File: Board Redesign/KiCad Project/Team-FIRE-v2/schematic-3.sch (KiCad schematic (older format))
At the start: 27 parts, among them IC2 BTS500601TEAAUMA2, U8 TPS82140SILR

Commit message: Starting complete BOM generation
- Finished schematic(s)
- Started BOM information assignment for final BOM sent to NASA
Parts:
- gave numbers to parts that had none: 24

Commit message: Fixed libraries, added BOM info to most components
- Fixed MCP1826T library to be a part of Team-Fire library (not separate)
- Deleted useless library files for various pieces (such as ImportGuides, etc.)
- Fixed inductor value specification for boost converter
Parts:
- removed U8: TPS82140SILR, SIL0008D_SMD, symbol sw_reg:TPS82140SILR
- removed U9: MCP1826T-3302E_DC, Package_TO_SOT_SMD:SOT-223-5, symbol Team-FIRE:MCP1826T-3302E_DC
- added IC?: MCP1826T-3302E_DC, Team-FIRE:SOT127P706X180-6N, symbol Team-FIRE:MCP1826T-3302E_DC
- added U?: TPS82140, Package_LGA:Texas_MicroSiP-8-1EP_2.8x3.0mm_P0.65mm_EP1.1x1.9mm_SMD_ThermalVias, symbol Regulator_Switching:TPS82140
- J10: Height 4.34 -> (none); Manufacturer (none) -> Taoglas; Manufacturer_Name Taoglas -> (none); Mouser Part Number 960-PCBMMCXFSTJACKHT -> (none); Mouser Price/Stock https://www.mouser.com/Search/Refine.aspx?Keyword=960-PCBMM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 -> (none); Supplier PN (none) -> 960-PCBMMCXFSTJACKHT
- J9: Height 1.25 -> (none); Manufacturer (none) -> Hirose; Manufacturer PN (none) -> U.FL-R-SMT(10); Manufacturer_Name Hirose -> (none); Manufacturer_Part_Number U.FL-R-SMT(10) -> (none); Mouser Price/Stock https://www.mouser.com/Search/Refine.aspx?Keyword=798-U.FL-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 -> (none)
- TP1, TP2, TP3, TP4, TP5, TP6, TP7, TP8: footprint (none) -> TestPoint:TestPoint_Pad_D1.5mm
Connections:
- wire segments 78 -> 73
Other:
- moved on the sheet: C32, C33, C34, C35, R21, R22, R24, R25, TP1, TP2, TP3, TP4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

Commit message: Made a lot of changes...
- Added symbol, footprint for Micro USB B connector
- Fixed Flash Memory schematic
- Added details for many components
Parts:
- gave numbers to parts that had none: 2
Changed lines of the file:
@@
 PWR_EN
 $Comp
-L Regulator_Switching:TPS82140 U?
+L Regulator_Switching:TPS82140 U8
 U 1 1 5EB31C18
 P 7100 1650
-F 0 "U?" H 7100 2117 50  0000 C CNN
+F 0 "U8" H 7100 2117 50  0000 C CNN
 F 1 "TPS82140" H 7100 2026 50  0000 C CNN
 F 2 "Package_LGA:Texas_MicroSiP-8-1EP_2.8x3.0mm_P0.65mm_EP1.1x1.9mm_SMD_ThermalVias" H 7100 1000 50  0001 C CNN
@@
 $EndComp
 $Comp
-L power:GND #PWR?
+L power:GND #PWR04
 U 1 1 5EB3DB22
 P 7100 2050
-F 0 "#PWR?" H 7100 1800 50  0001 C CNN
+F 0 "#PWR04" H 7100 1800 50  0001 C CNN
 F 1 "GND" H 7105 1877 50  0000 C CNN
 F 2 "" H 7100 2050 50  0001 C CNN
@@
 	6600 1850 6600 1950
 $Comp
-L power:GND #PWR?
+L power:GND #PWR07
 U 1 1 5EB42A65
 P 6600 2250
-F 0 "#PWR?" H 6600 2000 50  0001 C CNN
+F 0 "#PWR07" H 6600 2000 50  0001 C CNN
 F 1 "GND" H 6605 2077 50  0000 C CNN
 F 2 "" H 6600 2250 50  0001 C CNN
@@
 Connection ~ 6500 1450
 $Comp
-L power:GND #PWR?
+L power:GND #PWR03
 U 1 1 5EB9233E
 P 6350 1850
-F 0 "#PWR?" H 6350 1600 50  0001 C CNN
+F 0 "#PWR03" H 6350 1600 50  0001 C CNN
 F 1 "GND" H 6355 1677 50  0000 C CNN
 F 2 "" H 6350 1850 50  0001 C CNN
@@
 Connection ~ 7800 1850
 $Comp
-L power:GND #PWR?
+L power:GND #PWR05
 U 1 1 5EBE5BFA
 P 7800 2200
-F 0 "#PWR?" H 7800 1950 50  0001 C CNN
+F 0 "#PWR05" H 7800 1950 50  0001 C CNN
 F 1 "GND" H 7805 2027 50  0000 C CNN
 F 2 "" H 7800 2200 50  0001 C CNN
@@
 	8100 2000 8100 2200
 $Comp
-L power:GND #PWR?
+L power:GND #PWR06
 U 1 1 5EBED12A
 P 8100 2200
-F 0 "#PWR?" H 8100 1950 50  0001 C CNN
+F 0 "#PWR06" H 8100 1950 50  0001 C CNN
 F 1 "GND" H 8105 2027 50  0000 C CNN
 F 2 "" H 8100 2200 50  0001 C CNN
@@
 	5950 2650 5950 950
 $Comp
-L Team-FIRE:MCP1826T-3302E_DC IC?
+L Team-FIRE:MCP1826T-3302E_DC IC1
 U 1 1 5EC035E3
 P 1650 3450
-F 0 "IC?" H 2350 3765 50  0000 C CNN
+F 0 "IC1" H 2350 3765 50  0000 C CNN
 F 1 "MCP1826T-3302E_DC" H 2350 3674 50  0000 C CNN
 F 2 "Team-FIRE:SOT127P706X180-6N" H 2900 3550 50  0001 L CNN
@@
 	3150 3650 3150 3750
 $Comp
-L power:GND #PWR?
+L power:GND #PWR08
 U 1 1 5EC0985C
 P 3150 3900
-F 0 "#PWR?" H 3150 3650 50  0001 C CNN
+F 0 "#PWR08" H 3150 3650 50  0001 C CNN
 F 1 "GND" H 3155 3727 50  0000 C CNN
 F 2 "" H 3150 3900 50  0001 C CNN

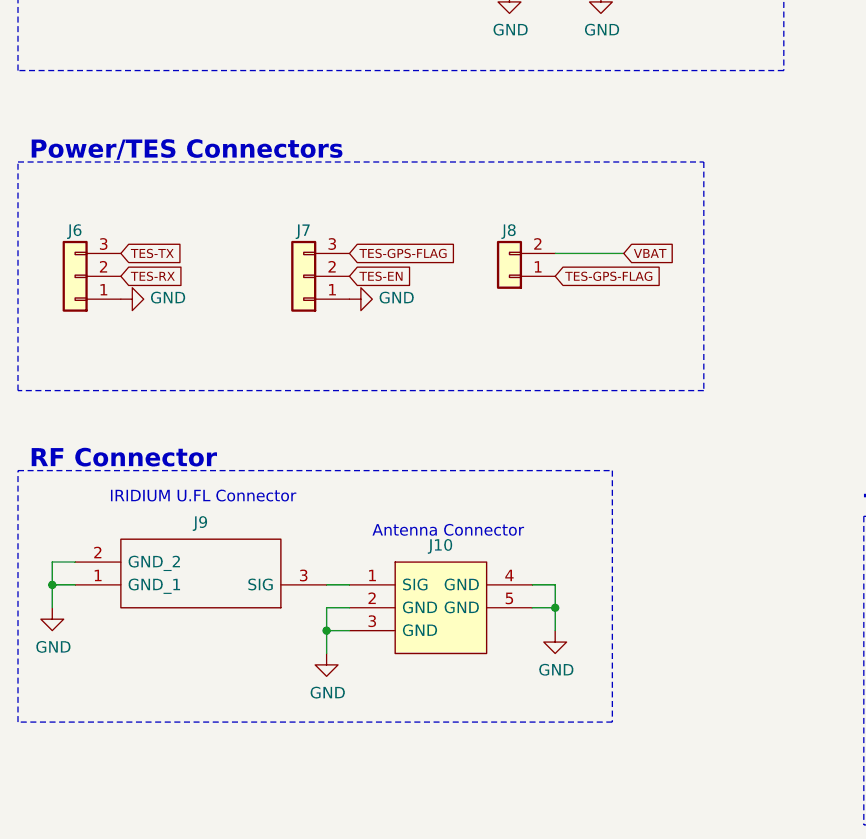
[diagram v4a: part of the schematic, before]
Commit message: Fixed alignment(s), added component details
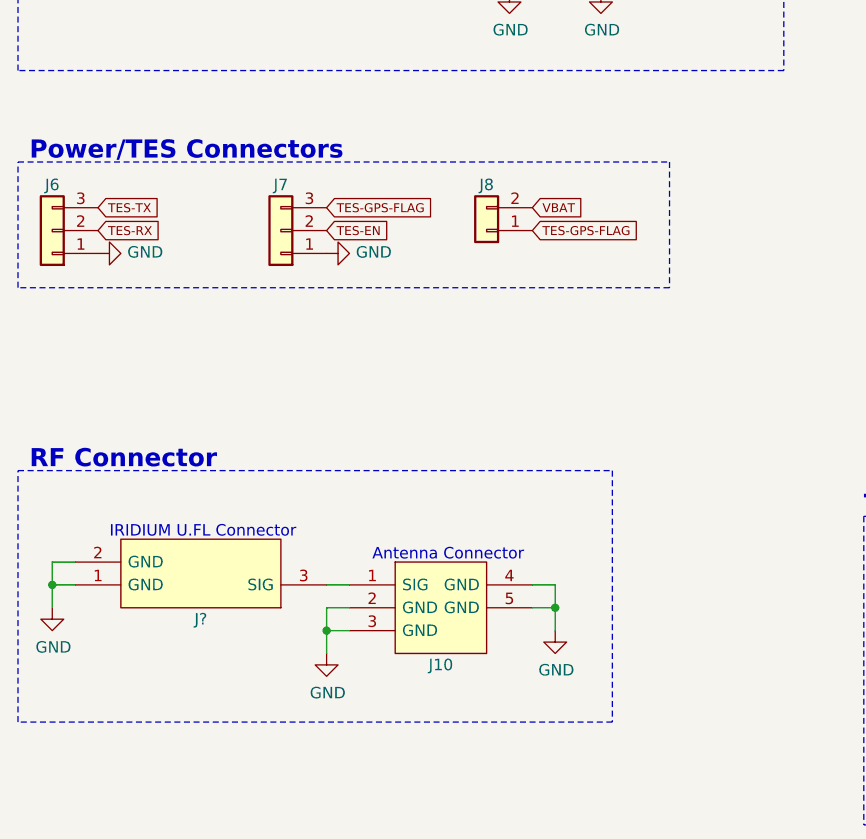
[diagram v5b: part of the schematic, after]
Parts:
- removed J9: U.FL-R-SMT_10_, Team-FIRE:UFLRSMT10, symbol Team-FIRE-v2-rescue:U.FL-R-SMT_10_-Team-FIRE
- added J?: U.FL-R-SMT_10_, UFLRSMT10, symbol Team-FIRE:U.FL-R-SMT_10_
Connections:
- net GND: now also J?.1 (GND), J?.2 (GND)
- net at J10.1 (SIG): now also J?.3 (SIG)
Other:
- moved on the sheet: J6, J7, J8
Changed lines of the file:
@@
 U 1 1 5EA814BB
 P 2400 1450
+AR Path="/5EA814BB" Ref="IC2"  Part="1"
+AR Path="/5E585515/5EA814BB" Ref="IC2"  Part="1"
 F 0 "IC2" H 2900 1715 50  0000 C CNN
 F 1 "BTS500601TEAAUMA2" H 2900 1624 50  0000 C CNN
@@
 L Connector_Generic:Conn_01x03 J6
 U 1 1 5EA3E857
-P 1250 5150
-F 0 "J6" H 1250 4950 50  0000 C CNN
-F 1 "Conn_01x03" H 1168 4916 50  0001 C CNN
-F 2 "Connector_JST:JST_SH_SM03B-SRSS-TB_1x03-1MP_P1.00mm_Horizontal" H 1250 5150 50  0001 C CNN
-F 3 "~" H 1250 5150 50  0001 C CNN
-F 4 "SM03B-SRSS-TB(LF)(SN)" H 1250 5150 50  0001 C CNN "MPN"
-	1    1250 5150
+P 1150 4950
+F 0 "J6" H 1150 4750 50  0000 C CNN
+F 1 "Conn_01x03" H 1068 4716 50  0001 C CNN
+F 2 "Connector_JST:JST_SH_SM03B-SRSS-TB_1x03-1MP_P1.00mm_Horizontal" H 1150 4950 50  0001 C CNN
+F 3 "~" H 1150 4950 50  0001 C CNN
+F 4 "SM03B-SRSS-TB(LF)(SN)" H 1150 4950 50  0001 C CNN "MPN"
+	1    1150 4950
 	-1   0    0    1
 $EndComp
@@
 L Connector_Generic:Conn_01x03 J7
 U 1 1 5EA3FD2C
-P 2250 5150
-F 0 "J7" H 2250 4950 50  0000 C CNN
-F 1 "Conn_01x03" H 2168 4916 50  0001 C CNN
-F 2 "Connector_JST:JST_SH_SM03B-SRSS-TB_1x03-1MP_P1.00mm_Horizontal" H 2250 5150 50  0001 C CNN
-F 3 "~" H 2250 5150 50  0001 C CNN
-F 4 "SM03B-SRSS-TB(LF)(SN)" H 2250 5150 50  0001 C CNN "MPN"
-	1    2250 5150
+P 2150 4950
+F 0 "J7" H 2150 4750 50  0000 C CNN
+F 1 "Conn_01x03" H 2068 4716 50  0001 C CNN
+F 2 "Connector_JST:JST_SH_SM03B-SRSS-TB_1x03-1MP_P1.00mm_Horizontal" H 2150 4950 50  0001 C CNN
+F 3 "~" H 2150 4950 50  0001 C CNN
+F 4 "SM03B-SRSS-TB(LF)(SN)" H 2150 4950 50  0001 C CNN "MPN"
+	1    2150 4950
 	-1   0    0    1
 $EndComp
-Text GLabel 1450 5050 2    39   Input ~ 0
+Text GLabel 1350 4850 2    39   Input ~ 0
 TES-TX
-Text GLabel 1450 5150 2    39   Input ~ 0
+Text GLabel 1350 4950 2    39   Input ~ 0
 TES-RX
 $Comp
 L power:GND #PWR0158
 U 1 1 5EA4D0AF
-P 1450 5250
-F 0 "#PWR0158" H 1450 5000 50  0001 C CNN
-F 1 "GND" V 1455 5122 50  0000 R CNN
-F 2 "" H 1450 5250 50  0001 C CNN
-F 3 "" H 1450 5250 50  0001 C CNN
-	1    1450 5250
+P 1350 5050
+F 0 "#PWR0158" H 1350 4800 50  0001 C CNN
+F 1 "GND" V 1355 4922 50  0000 R CNN
+F 2 "" H 1350 5050 50  0001 C CNN
+F 3 "" H 1350 5050 50  0001 C CNN
+	1    1350 5050
 	0    -1   -1   0
 $EndComp
-Text GLabel 2450 5050 2    39   Input ~ 0
+Text GLabel 2350 4850 2    39   Input ~ 0
 TES-GPS-FLAG
-Text GLabel 2450 5150 2    39   Input ~ 0
+Text GLabel 2350 4950 2    39   Input ~ 0
 TES-EN
 $Comp
 L power:GND #PWR0159
 U 1 1 5EA5A5FD
-P 2450 5250
-F 0 "#PWR0159" H 2450 5000 50  0001 C CNN
-F 1 "GND" V 2455 5122 50  0000 R CNN
-F 2 "" H 2450 5250 50  0001 C CNN
-F 3 "" H 2450 5250 50  0001 C CNN
-	1    2450 5250
+P 2350 5050
+F 0 "#PWR0159" H 2350 4800 50  0001 C CNN
+F 1 "GND" V 2355 4922 50  0000 R CNN
+F 2 "" H 2350 5050 50  0001 C CNN
+F 3 "" H 2350 5050 50  0001 C CNN
+	1    2350 5050
 	0    -1   -1   0
-$EndComp
-$Comp
-L Team-FIRE-v2-rescue:U.FL-R-SMT_10_-Team-FIRE J?
-U 1 1 5EA3C18D
-P 2350 6500
-AR Path="/5EA3C18D" Ref="J?"  Part="1"
-AR Path="/5E585515/5EA3C18D" Ref="J9"  Part="1"
-F 0 "J9" H 2900 6227 50  0000 C CNN
-F 1 "U.FL-R-SMT_10_" H 2900 6226 50  0001 C CNN
-F 2 "Team-FIRE:UFLRSMT10" H 3300 6600 50  0001 L CNN
-F 3 "https://media.digikey.com/pdf/Data%20Sheets/Hirose%20PDFs/UFL%20Series.pdf" H 3300 6500 50  0001 L CNN
-F 4 "RF Connectors / Coaxial Connectors U.FL RECEPTACLE SMT GLD M CONT REEL" H 3300 6400 50  0001 L CNN "Description"
-F 5 "Hirose" H 3300 6200 50  0001 L CNN "Manufacturer"
-F 6 "U.FL-R-SMT(10)" H 3300 6100 50  0001 L CNN "Manufacturer PN"
-F 7 "798-U.FL-R-SMT10" H 3300 6000 50  0001 L CNN "MPN"
-	1    2350 6500
-	-1   0    0    1
 $EndComp
 $Comp
@@
 U 1 1 5EA3CD82
 P 2450 6500
-F 0 "J10" H 2850 6673 50  0000 C CNN
+AR Path="/5EA3CD82" Ref="J10"  Part="1"
+AR Path="/5E585515/5EA3CD82" Ref="J10"  Part="1"
+F 0 "J10" H 2850 6150 50  0000 C CNN
 F 1 "PCB.MMCX.F.ST.SMT.JACK.HT" H 2850 6674 50  0001 C CNN
 F 2 "Team-FIRE:PCBMMCXFSTSMTJACKHT" H 3100 6600 50  0001 L CNN
@@
 	1    0    0    -1
 $EndComp
-Text Notes 1400 6150 0    50   ~ 0
+Text Notes 1400 6300 0    50   ~ 0
 IRIDIUM U.FL Connector
-Text Notes 2550 6300 0    50   ~ 0
+Text Notes 2550 6400 0    50   ~ 0
 Antenna Connector\n
 Wire Notes Line
@@
 L Connector_Generic:Conn_01x02 J8
 U 1 1 5EB75BFF
-P 3150 5150
-F 0 "J8" H 3150 4950 50  0000 C CNN
-F 1 "Conn_01x02" H 3068 4916 50  0001 C CNN
-F 2 "Team-FIRE:43650-0200" H 3150 5150 50  0001 C CNN
-F 3 "~" H 3150 5150 50  0001 C CNN
-F 4 "43650-0200" H 3150 5150 50  0001 C CNN "MPN"
-	1    3150 5150
+P 3050 4950
+F 0 "J8" H 3050 4750 50  0000 C CNN
+F 1 "Conn_01x02" H 2968 4716 50  0001 C CNN
+F 2 "Team-FIRE:43650-0200" H 3050 4950 50  0001 C CNN
+F 3 "~" H 3050 4950 50  0001 C CNN
+F 4 "43650-0200" H 3050 4950 50  0001 C CNN "MPN"
+	1    3050 4950
 	-1   0    0    1
 $EndComp
-Text GLabel 3650 5050 2    39   Input ~ 0
-VBAT
-Text GLabel 3350 5150 2    39   Input ~ 0
+Text GLabel 3250 4950 2    39   Input ~ 0
 TES-GPS-FLAG
 $Comp
@@
 Text Notes 5950 950  0    79   ~ 16
 8V to 5V Switching Regulator
-Wire Wire Line
-	3350 5050 3650 5050
-Wire Notes Line
-	1000 4650 4000 4650
-Wire Notes Line
-	4000 4650 4000 5650
-Wire Notes Line
-	4000 5650 1000 5650
-Wire Notes Line
-	1000 5650 1000 4650
 Text GLabel 6250 1450 0    39   Input ~ 0
 VBAT
@@
 Wire Wire Line
 	3350 6600 3350 6700
+$Comp
+L Team-FIRE:U.FL-R-SMT_10_ J?
+U 1 1 5EB7B21D
+P 2350 6500
+F 0 "J?" H 2900 6650 50  0000 C CNN
+F 1 "U.FL-R-SMT_10_" H 2900 6226 50  0001 C CNN
+F 2 "UFLRSMT10" H 3300 6600 50  0001 L CNN
+F 3 "https://media.digikey.com/pdf/Data%20Sheets/Hirose%20PDFs/UFL%20Series.pdf" H 3300 6500 50  0001 L CNN
+F 4 "RF Connectors / Coaxial Connectors U.FL RECEPTACLE SMT GLD M CONT REEL" H 3300 6400 50  0001 L CNN "Description"
+F 5 "1.25" H 3300 6300 50  0001 L CNN "Height"
+F 6 "Hirose" H 3300 6200 50  0001 L CNN "Manufacturer_Name"
+F 7 "U.FL-R-SMT(10)" H 3300 6100 50  0001 L CNN "Manufacturer_Part_Number"
+F 8 "798-U.FL-R-SMT10" H 3300 6000 50  0001 L CNN "Mouser Part Number"
+F 9 "https://www.mouser.com/Search/Refine.aspx?Keyword=798-U.FL-R-SMT10" H 3300 5900 50  0001 L CNN "Mouser Price/Stock"
+	1    2350 6500
+	-1   0    0    1
+$EndComp
+Text GLabel 3250 4850 2    39   Input ~ 0
+VBAT
+Wire Notes Line
+	1000 4650 3850 4650
+Wire Notes Line
+	3850 4650 3850 5200
+Wire Notes Line
+	3850 5200 1000 5200
+Wire Notes Line
+	1000 5200 1000 4650
 $EndSCHEMATC
